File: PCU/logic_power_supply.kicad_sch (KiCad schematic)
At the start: 54 parts, among them IC34 AP63205WU-7, IC35 AP63203WU-7, J16 B2B-PH-K-S, J17 B2B-PH-K-S, J18 B2B-PH-K-S

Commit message: PSU Blocks Routed
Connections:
- net +3.3V_Logic: now also C219.2, C222.2, FB2.1, IC35.1 (FB), L5.2, TP9.1; no longer C229.2, C230.2, D47.1 (K), D48.1 (K), R258.1, R259.2, TP11.1
- new net +3.3V_Logic_filtered: C229.2, C230.2, D47.1 (K), D48.1 (K), R258.1, R259.2, TP11.1
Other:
- note added: "+3.3V_Logic_filtered Mesurement"
- note removed: "+3.3V_Logic Mesurement"
- moved on the sheet: FB2, R258
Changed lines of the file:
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@@
 		)
 	)
-	(text "+3.3V_Logic Mesurement"
+	(text "+3.3V_Logic_filtered Mesurement"
 		(exclude_from_sim no)
 		(at 254.254 203.2 0)
@@
 	)
 	(junction
+		(at 195.58 88.9)
+		(diameter 0)
+		(color 0 0 0 0)
+	)
+	(junction
 		(at 73.66 139.7)
 		(diameter 0)
@@
 	(wire
 		(pts
+			(xy 195.58 88.9) (xy 204.47 88.9)
+		)
+		(stroke
+			(width 0)
+			(type default)
+		)
+	)
+	(wire
+		(pts
 			(xy 49.53 237.49) (xy 49.53 240.03)
 		)
@@
 	(wire
 		(pts
-			(xy 204.47 88.9) (xy 214.63 88.9)
+			(xy 212.09 88.9) (xy 218.44 88.9)
 		)
 		(stroke
@@
 	(wire
 		(pts
+			(xy 195.58 86.36) (xy 195.58 88.9)
+		)
+		(stroke
+			(width 0)
+			(type default)
+		)
+	)
+	(wire
+		(pts
 			(xy 114.3 33.02) (xy 119.38 33.02)
 		)
@@
 	(wire
 		(pts
-			(xy 222.25 88.9) (xy 233.68 88.9)
+			(xy 226.06 88.9) (xy 233.68 88.9)
 		)
 		(stroke
@@
 	(wire
 		(pts
-			(xy 180.34 88.9) (xy 196.85 88.9)
+			(xy 180.34 88.9) (xy 195.58 88.9)
 		)
 		(stroke
@@
 	)
 	(symbol
+		(lib_id "power:+3.3V")
+		(at 195.58 86.36 0)
+		(unit 1)
+		(exclude_from_sim no)
+		(in_bom yes)
+		(on_board yes)
+		(dnp no)
+		(fields_autoplaced yes)
+		(property "Reference" "#PWR0496"
+			(at 195.58 90.17 0)
+			(effects
+				(font
+					(size 1.27 1.27)
+				)
+				(hide yes)
+			)
+		)
+		(property "Value" "+3.3V_Logic"
+			(at 195.58 81.28 0)
+			(effects
+				(font
+					(size 1.27 1.27)
+				)
+			)
+		)
+		(property "Footprint" ""
+			(at 195.58 86.36 0)
+			(effects
+				(font
+					(size 1.27 1.27)
+				)
+				(hide yes)
+			)
+		)
+		(property "Datasheet" ""
+			(at 195.58 86.36 0)
+			(effects
+				(font
+					(size 1.27 1.27)
+				)
+				(hide yes)
+			)
+		)
+		(property "Description" "Power symbol creates a global label with name \"+3.3V\""
+			(at 195.58 86.36 0)
+			(effects
+				(font
+					(size 1.27 1.27)
+				)
+				(hide yes)
+			)
+		)
+		(pin "1"
+		)
+		(instances
+			(project "PCU"
+				(path "/c5277b98-916c-45ac-b199-6b9ee16008ba/8122c3c1-3842-43f9-aad7-aa03fb26189b"
+					(reference "#PWR0496")
+					(unit 1)
+				)
+			)
+		)
+	)
+	(symbol
 		(lib_id "BassingaLib_SMPS:AP63200WU-7")
 		(at 100.33 39.37 0)
@@
 			)
 		)
-		(property "Value" "+3.3V_Logic"
+		(property "Value" "+3.3V_Logic_filtered"
 			(at 274.32 76.2 0)
 			(effects
@@
 		(on_board yes)
 		(dnp no)
-		(fields_autoplaced yes)
 		(property "Reference" "#PWR0430"
 			(at 320.04 113.03 0)
@@
 		)
 		(property "Value" "+3.3V_Logic"
-			(at 320.04 104.14 0)
+			(at 314.452 104.14 0)
 			(effects
 				(font
 					(size 1.27 1.27)
 				)
+				(justify left)
 			)
 		)
@@
 			)
 		)
-		(property "Value" "+3.3V_Logic"
+		(property "Value" "+3.3V_Logic_filtered"
 			(at 115.57 213.36 0)
 			(effects
@@
 			)
 		)
-		(property "Value" "+3.3V_Logic"
+		(property "Value" "+3.3V_Logic_filtered"
 			(at 49.53 214.63 0)
 			(effects
@@
 		(on_board yes)
 		(dnp no)
-		(fields_autoplaced yes)
 		(property "Reference" "#PWR0436"
 			(at 375.92 195.58 0)
@@
 		)
 		(property "Value" "+3.3V_Logic"
-			(at 375.92 186.69 0)
+			(at 369.57 186.944 0)
 			(effects
 				(font
 					(size 1.27 1.27)
 				)
+				(justify left)
 			)
 		)
@@
 	(symbol
 		(lib_id "Device:R")
-		(at 218.44 88.9 270)
+		(at 222.25 88.9 270)
 		(mirror x)
 		(unit 1)
@@
 		(dnp no)
 		(property "Reference" "R258"
-			(at 216.662 91.948 90)
+			(at 220.472 91.948 90)
 			(effects
 				(font
@@
 		)
 		(property "Value" "0.22R 1%"
-			(at 215.138 85.598 90)
+			(at 218.948 85.598 90)
 			(effects
 				(font
@@
 		)
 		(property "Footprint" "Resistor_SMD:R_0805_2012Metric"
-			(at 218.44 90.678 90)
+			(at 222.25 90.678 90)
 			(effects
 				(font
@@
 		)
 		(property "Datasheet" "~"
-			(at 218.44 88.9 0)
+			(at 222.25 88.9 0)
 			(effects
 				(font
@@
 		)
 		(property "Description" "Resistor"
-			(at 218.44 88.9 0)
+			(at 222.25 88.9 0)
 			(effects
 				(font
@@
 		)
 		(property "Manufacturer_Name" "YAGEO"
-			(at 218.44 88.9 0)
+			(at 222.25 88.9 0)
 			(effects
 				(font
@@
 		)
 		(property "Manufacturer_Part_Number" "RL0805FR-7W0R22L"
-			(at 218.44 88.9 0)
+			(at 222.25 88.9 0)
 			(effects
 				(font
@@
 		)
 		(property "Packaging" "0805 (2012mm)"
-			(at 218.44 88.9 0)
+			(at 222.25 88.9 0)
 			(effects
 				(font
@@
 	(symbol
 		(lib_id "Device:FerriteBead")
-		(at 200.66 88.9 90)
+		(at 208.28 88.9 90)
 		(unit 1)
 		(exclude_from_sim no)
@@
 		(fields_autoplaced yes)
 		(property "Reference" "FB2"
-			(at 200.6092 81.28 90)
+			(at 208.2292 81.28 90)
 			(effects
 				(font
@@
 		)
 		(property "Value" "FerriteBead"
-			(at 200.6092 83.82 90)
+			(at 208.2292 83.82 90)
 			(effects
 				(font
@@
 		)
 		(property "Footprint" "Inductor_SMD:L_0805_2012Metric"
-			(at 200.66 90.678 90)
+			(at 208.28 90.678 90)
 			(effects
 				(font
@@
 		)
 		(property "Datasheet" "~"
-			(at 200.66 88.9 0)
+			(at 208.28 88.9 0)
 			(effects
 				(font
@@
 		)
 		(property "Description" "Ferrite bead"
-			(at 200.66 88.9 0)
+			(at 208.28 88.9 0)
 			(effects
 				(font
@@
 		)
 		(property "Manufacturer_Name" "TDK"
-			(at 200.66 88.9 90)
+			(at 208.28 88.9 90)
 			(effects
 				(font
@@
 		)
 		(property "Manufacturer_Part_Number" "MPZ2012S601AT000"
-			(at 200.66 88.9 90)
+			(at 208.28 88.9 90)
 			(effects
 				(font
@@
 		)
 		(property "Packaging" "0805 (2012mm)"
-			(at 200.66 88.9 90)
+			(at 208.28 88.9 90)
 			(effects
 				(font
@@
 			)
 		)
-		(property "Value" "+3.3V_Logic"
+		(property "Value" "+3.3V_Logic_filtered"
 			(at 238.76 213.36 0)
 			(effects

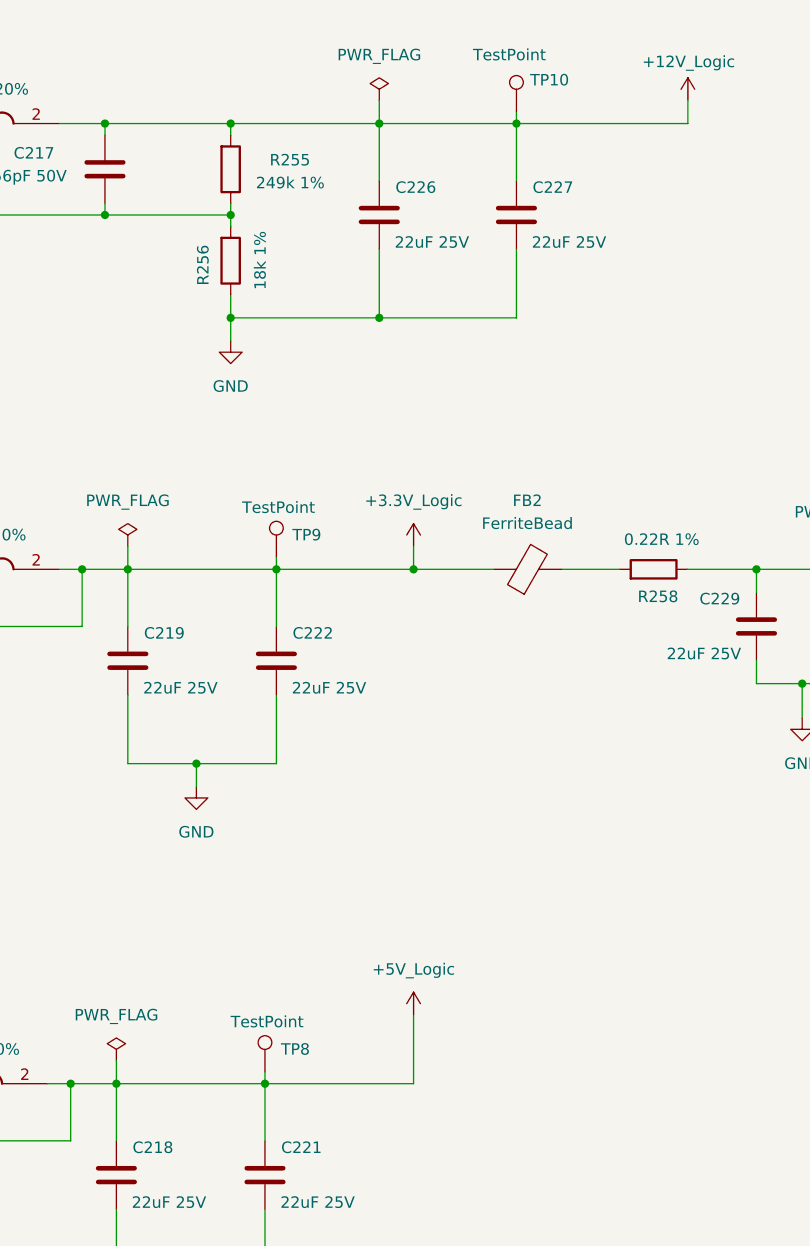
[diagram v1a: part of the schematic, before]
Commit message: All components placed
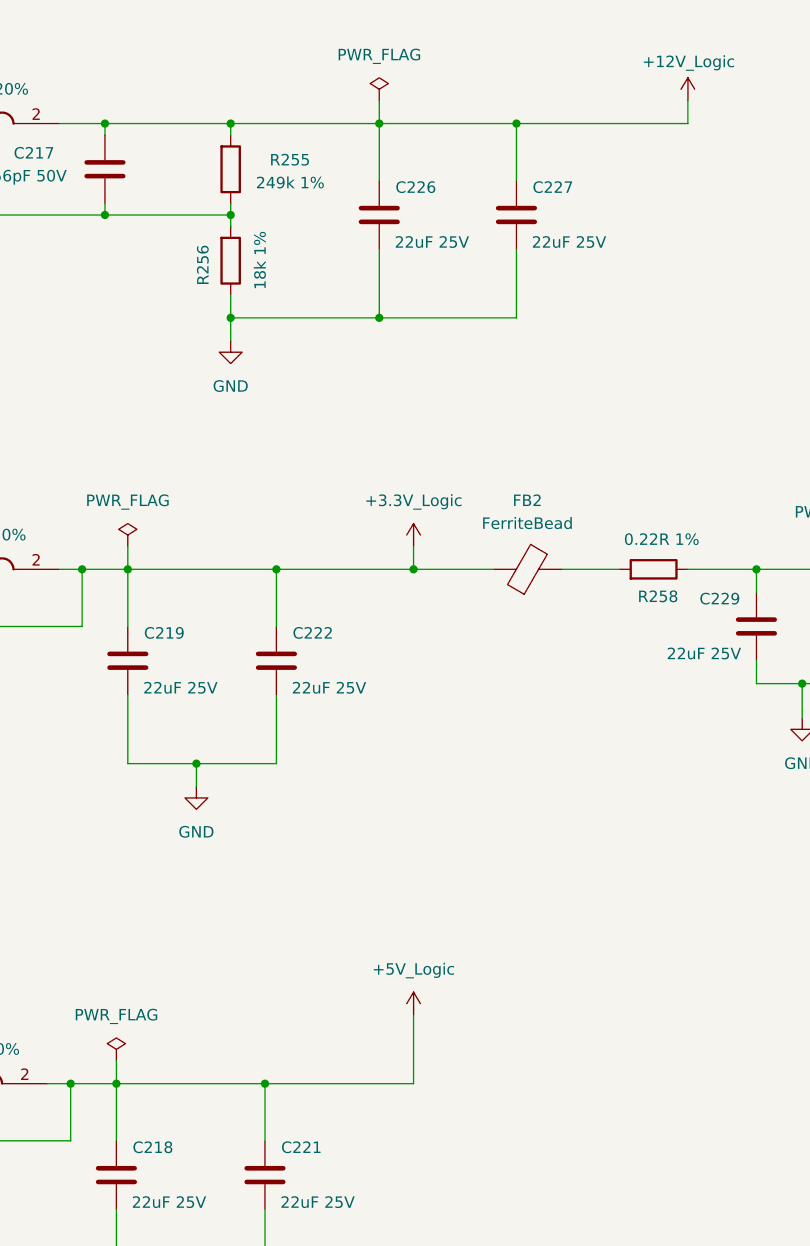
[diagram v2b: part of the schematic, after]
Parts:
- removed TP10, TP8, TP9: TestPoint, TestPoint:TestPoint_Pad_D1.0mm, symbol Connector:TestPoint
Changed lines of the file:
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@@
 	(wire
 		(pts
-			(xy 180.34 87.63) (xy 180.34 88.9)
-		)
-		(stroke
-			(width 0)
-			(type default)
-		)
-	)
-	(wire
-		(pts
 			(xy 130.81 39.37) (xy 135.89 39.37)
 		)
@@
 	(wire
 		(pts
-			(xy 207.01 38.1) (xy 207.01 39.37)
-		)
-		(stroke
-			(width 0)
-			(type default)
-		)
-	)
-	(wire
-		(pts
 			(xy 175.26 60.96) (xy 191.77 60.96)
 		)
@@
 	(wire
 		(pts
-			(xy 179.07 144.78) (xy 179.07 146.05)
-		)
-		(stroke
-			(width 0)
-			(type default)
-		)
-	)
-	(wire
-		(pts
 			(xy 85.09 33.02) (xy 90.17 33.02)
 		)
@@
 	)
 	(symbol
-		(lib_id "Connector:TestPoint")
-		(at 207.01 38.1 0)
-		(unit 1)
-		(exclude_from_sim no)
-		(in_bom yes)
-		(on_board yes)
-		(dnp no)
-		(property "Reference" "TP10"
-			(at 208.534 34.544 0)
-			(effects
-				(font
-					(size 1.27 1.27)
-				)
-				(justify left)
-			)
-		)
-		(property "Value" "TestPoint"
-			(at 202.184 31.75 0)
-			(effects
-				(font
-					(size 1.27 1.27)
-				)
-				(justify left)
-			)
-		)
-		(property "Footprint" "TestPoint:TestPoint_Pad_D1.0mm"
-			(at 212.09 38.1 0)
-			(effects
-				(font
-					(size 1.27 1.27)
-				)
-				(hide yes)
-			)
-		)
-		(property "Datasheet" "~"
-			(at 212.09 38.1 0)
-			(effects
-				(font
-					(size 1.27 1.27)
-				)
-				(hide yes)
-			)
-		)
-		(property "Description" "test point"
-			(at 207.01 38.1 0)
-			(effects
-				(font
-					(size 1.27 1.27)
-				)
-				(hide yes)
-			)
-		)
-		(pin "1"
-		)
-		(instances
-			(project "PCU"
-				(path "/c5277b98-916c-45ac-b199-6b9ee16008ba/8122c3c1-3842-43f9-aad7-aa03fb26189b"
-					(reference "TP10")
-					(unit 1)
-				)
-			)
-		)
-	)
-	(symbol
 		(lib_id "power:GND")
 		(at 171.45 113.03 0)
@@
 	)
 	(symbol
-		(lib_id "Connector:TestPoint")
-		(at 179.07 144.78 0)
-		(unit 1)
-		(exclude_from_sim no)
-		(in_bom yes)
-		(on_board yes)
-		(dnp no)
-		(property "Reference" "TP8"
-			(at 180.848 142.24 0)
-			(effects
-				(font
-					(size 1.27 1.27)
-				)
-				(justify left)
-			)
-		)
-		(property "Value" "TestPoint"
-			(at 175.26 139.192 0)
-			(effects
-				(font
-					(size 1.27 1.27)
-				)
-				(justify left)
-			)
-		)
-		(property "Footprint" "TestPoint:TestPoint_Pad_D1.0mm"
-			(at 184.15 144.78 0)
-			(effects
-				(font
-					(size 1.27 1.27)
-				)
-				(hide yes)
-			)
-		)
-		(property "Datasheet" "~"
-			(at 184.15 144.78 0)
-			(effects
-				(font
-					(size 1.27 1.27)
-				)
-				(hide yes)
-			)
-		)
-		(property "Description" "test point"
-			(at 179.07 144.78 0)
-			(effects
-				(font
-					(size 1.27 1.27)
-				)
-				(hide yes)
-			)
-		)
-		(pin "1"
-		)
-		(instances
-			(project "PCU"
-				(path "/c5277b98-916c-45ac-b199-6b9ee16008ba/8122c3c1-3842-43f9-aad7-aa03fb26189b"
-					(reference "TP8")
-					(unit 1)
-				)
-			)
-		)
-	)
-	(symbol
 		(lib_id "power:+3.3V")
 		(at 318.77 52.07 0)
@@
 					(unit 1)
 				)
-			)
-		)
-	)
-	(symbol
-		(lib_id "Connector:TestPoint")
-		(at 180.34 87.63 0)
-		(unit 1)
-		(exclude_from_sim no)
-		(in_bom yes)
-		(on_board yes)
-		(dnp no)
-		(property "Reference" "TP9"
-			(at 182.118 85.09 0)
-			(effects
-				(font
-					(size 1.27 1.27)
-				)
-				(justify left)
-			)
-		)
-		(property "Value" "TestPoint"
-			(at 176.53 82.042 0)
-			(effects
-				(font
-					(size 1.27 1.27)
-				)
-				(justify left)
-			)
-		)
-		(property "Footprint" "TestPoint:TestPoint_Pad_D1.0mm"
-			(at 185.42 87.63 0)
-			(effects
-				(font
-					(size 1.27 1.27)
-				)
-				(hide yes)
-			)
-		)
-		(property "Datasheet" "~"
-			(at 185.42 87.63 0)
-			(effects
-				(font
-					(size 1.27 1.27)
-				)
-				(hide yes)
-			)
-		)
-		(property "Description" "test point"
-			(at 180.34 87.63 0)
-			(effects
-				(font
-					(size 1.27 1.27)
-				)
-				(hide yes)
-			)
-		)
-		(pin "1"
-		)
-		(instances
-			(project "PCU"
-				(path "/c5277b98-916c-45ac-b199-6b9ee16008ba/8122c3c1-3842-43f9-aad7-aa03fb26189b"
-					(reference "TP9")
-					(unit 1)
-				)

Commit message: Components library added
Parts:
- TP11: now left out of the parts list
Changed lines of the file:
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@@
 		(unit 1)
 		(exclude_from_sim no)
-		(in_bom yes)
+		(in_bom no)
 		(on_board yes)
 		(dnp no)

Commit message: Fly controller design started
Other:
- company: BASSINGA Lab -> BASSINGA_LAB
- title: (none) -> Propulsion Control Unit
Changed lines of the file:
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@@
 	(paper "A3")
 	(title_block
+		(title "Propulsion Control Unit")
 		(date "2025-05-21")
 		(rev "v1.0")
-		(company "BASSINGA Lab")
+		(company "BASSINGA_LAB")
+		(comment 1 "Copyright © 2025 Andresse Brisel BASSINGA ")
 	)
 	(rectangle
